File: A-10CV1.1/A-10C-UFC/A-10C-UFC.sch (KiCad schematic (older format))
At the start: 42 parts, among them J1 Conn_01x08_MountingPin, J2 Conn_01x10_MountingPin, J3 Conn_01x06_MountingPin, J4 Conn_01x15_Female, J5 Conn_01x15_Female, SW1 SW_Push, SW10 SW_Push, SW11 SW_Push, SW12 SW_Push, SW13 SW_Push, SW14 SW_Push, SW15 SW_Push, SW16 SW_Push, SW17 SW_Push, SW18 SW_Push, SW19 SW_Push, SW2 SW_Push, SW20 SW_Push, SW21 SW_Push, SW22 SW_Push, SW23 SW_Push, SW24 SW_Push, SW25 SW_Push, SW26 SW_Push, SW27 SW_Push, SW28 SW_Push, SW29 SW_Push, SW3 SW_Push, SW30 SW_Push, SW31 SW_Push, SW32 SW_Push, SW33 SW_Push, SW34 SW_Push, SW35 SW_Push, SW4 SW_Push, SW5 SW_Push, SW6 SW_Push, SW7 SW_Push, SW8 SW_Push, SW9 SW_Push

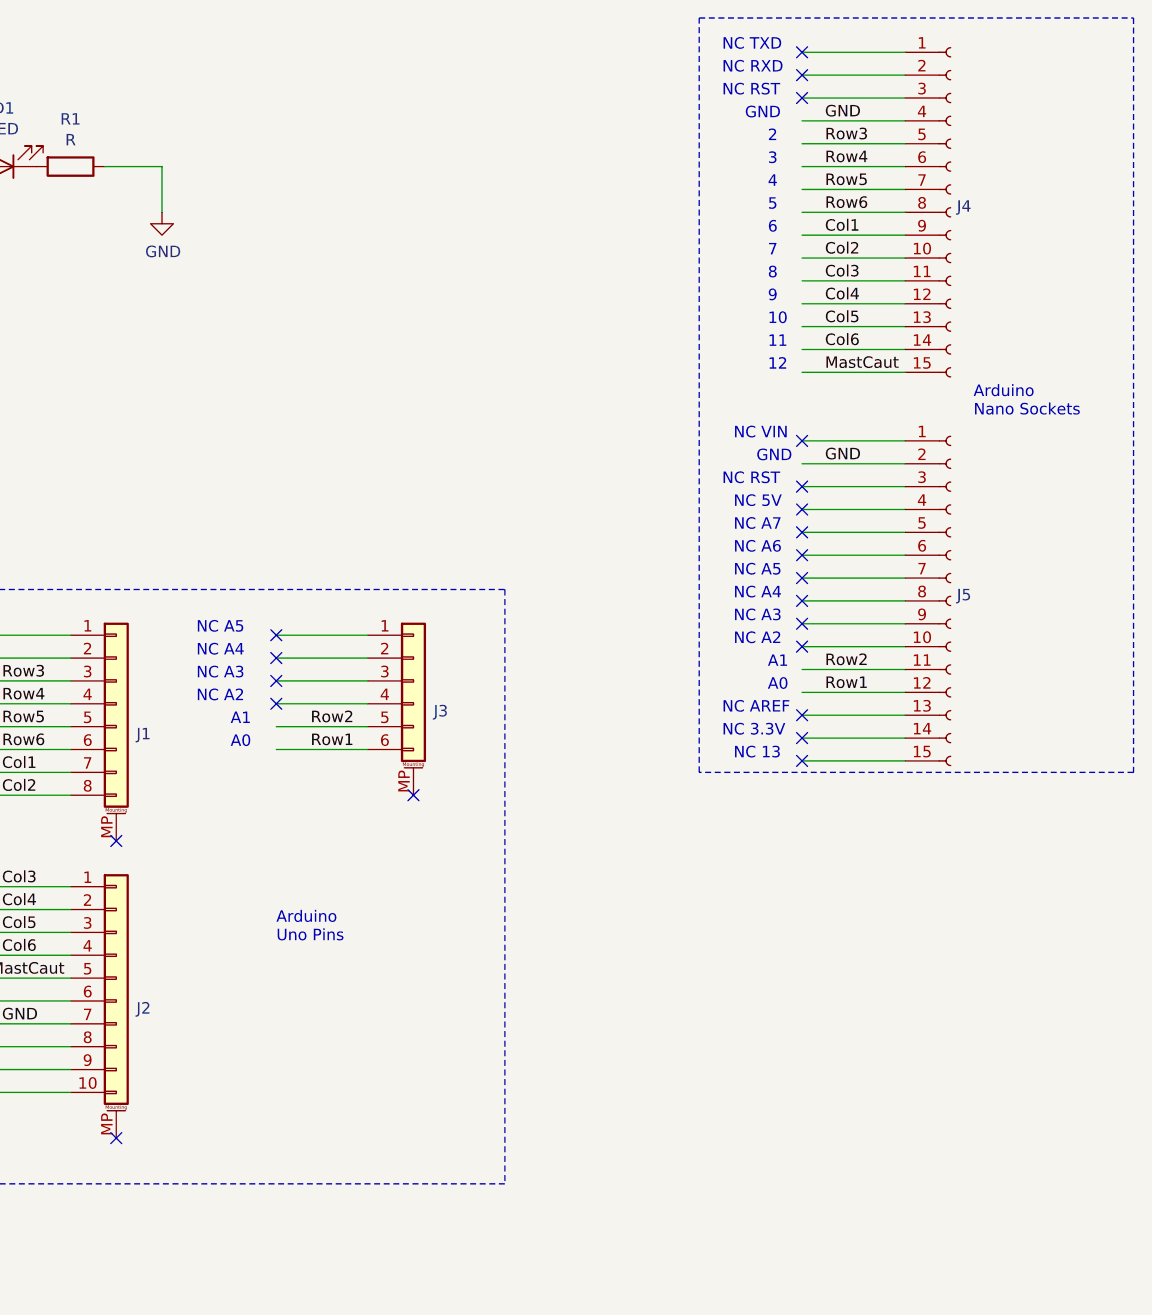
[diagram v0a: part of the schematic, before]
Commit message: Updated for multi aircraft capability.  Added wiring and code.
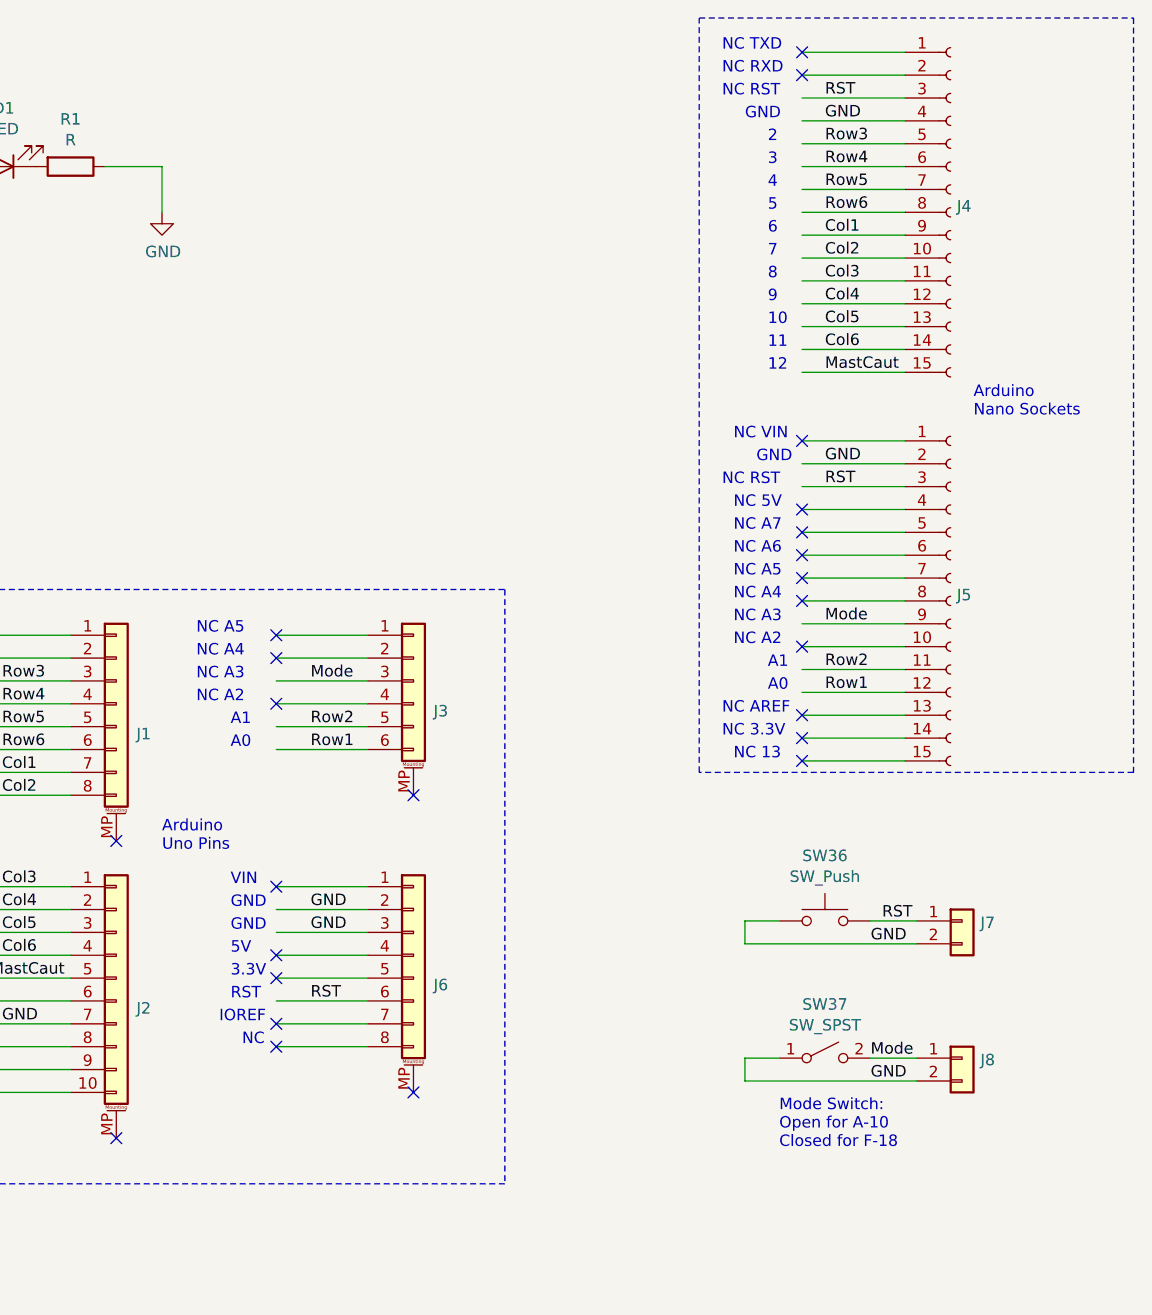
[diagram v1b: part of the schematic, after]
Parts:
- added J6: Conn_01x08_MountingPin, Connector_PinHeader_2.54mm:PinHeader_1x08_P2.54mm_Vertical, symbol Connector_Generic_MountingPin:Conn_01x08_MountingPin
- added J7, J8: Conn_01x02, Connector_JST:JST_XH_B02B-XH-A_1x02_P2.50mm_Vertical, symbol Connector_Generic:Conn_01x02
- added SW36: SW_Push, symbol Switch:SW_Push
- added SW37: SW_SPST, symbol Switch:SW_SPST
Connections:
- net labels added: Mode, RST
- wire segments 162 -> 178
- no-connect marks 28 -> 30
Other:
- note added: "3.3V"
- note added: "5V"
- note added: "IOREF"
- note added: "Mode Switch:\nOpen for A-10\nClosed for F-18"
- note added: "NC"
- note added: "RST"
- note added: "VIN"
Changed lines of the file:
@@
 Wire Notes Line
 	6500 5900 6500 3300
-Text Notes 8300 4850 0    50   ~ 0
+Text Notes 7800 4450 0    50   ~ 0
 Arduino\nUno Pins
 Text Notes 3200 6750 0    50   ~ 0
 Row  Digital Pins (A0,A1,2,3,4,5)\nCol Digital Pins (6,7,8,9,10,11)\n\nLED Output for Master Caution, Pin 12\n\nDesigned for plug in compatibility with \nArduino UNO and Nano
 NoConn ~ 10600 2650
-NoConn ~ 10600 2850
 NoConn ~ 10600 2950
 NoConn ~ 10600 3050
@@
 NoConn ~ 10600 3250
 NoConn ~ 10600 3350
-NoConn ~ 10600 3450
 NoConn ~ 10600 3550
 NoConn ~ 10600 3850
@@
 NoConn ~ 10600 950
 NoConn ~ 10600 1050
-NoConn ~ 10600 1150
 NoConn ~ 7000 3500
 NoConn ~ 7000 3600
 NoConn ~ 8300 3500
 NoConn ~ 8300 3600
-NoConn ~ 8300 3700
 NoConn ~ 8300 3800
 NoConn ~ 7600 4400
@@
 NoConn ~ 7000 5300
 NoConn ~ 7000 5100
+$Comp
+L Connector_Generic:Conn_01x02 J7
+U 1 1 5D473A0F
+P 11300 4750
+F 0 "J7" H 11380 4742 50  0000 L CNN
+F 1 "Conn_01x02" H 11380 4651 50  0001 L CNN
+F 2 "Connector_JST:JST_XH_B02B-XH-A_1x02_P2.50mm_Vertical" H 11300 4750 50  0001 C CNN
+F 3 "~" H 11300 4750 50  0001 C CNN
+	1    11300 4750
+	1    0    0    -1
+$EndComp
+$Comp
+L Connector_Generic:Conn_01x02 J8
+U 1 1 5D473B23
+P 11300 5350
+F 0 "J8" H 11380 5342 50  0000 L CNN
+F 1 "Conn_01x02" H 11380 5251 50  0001 L CNN
+F 2 "Connector_JST:JST_XH_B02B-XH-A_1x02_P2.50mm_Vertical" H 11300 5350 50  0001 C CNN
+F 3 "~" H 11300 5350 50  0001 C CNN
+	1    11300 5350
+	1    0    0    -1
+$EndComp
+$Comp
+L Switch:SW_Push SW36
+U 1 1 5D473BB8
+P 10700 4750
+F 0 "SW36" H 10700 5035 50  0000 C CNN
+F 1 "SW_Push" H 10700 4944 50  0000 C CNN
+F 2 "" H 10700 4950 50  0001 C CNN
+F 3 "" H 10700 4950 50  0001 C CNN
+	1    10700 4750
+	1    0    0    -1
+$EndComp
+$Comp
+L Switch:SW_SPST SW37
+U 1 1 5D473C67
+P 10700 5350
+F 0 "SW37" H 10700 5585 50  0000 C CNN
+F 1 "SW_SPST" H 10700 5494 50  0000 C CNN
+F 2 "" H 10700 5350 50  0001 C CNN
+F 3 "" H 10700 5350 50  0001 C CNN
+	1    10700 5350
+	1    0    0    -1
+$EndComp
+Wire Wire Line
+	11100 4750 10900 4750
+Wire Wire Line
+	10350 4750 10350 4850
+Wire Wire Line
+	10350 4850 11100 4850
+Wire Wire Line
+	10350 4750 10500 4750
+Wire Wire Line
+	11100 5350 10900 5350
+Wire Wire Line
+	10500 5350 10350 5350
+Wire Wire Line
+	10350 5350 10350 5450
+Wire Wire Line
+	10350 5450 11100 5450
+Text Label 10900 5450 0    50   ~ 0
+GND
+Text Label 10900 4850 0    50   ~ 0
+GND
+$Comp
+L Connector_Generic_MountingPin:Conn_01x08_MountingPin J6
+U 1 1 5D4991C7
+P 8900 4900
+F 0 "J6" H 8988 4770 50  0000 L CNN
+F 1 "Conn_01x08_MountingPin" H 8987 4725 50  0001 L CNN
+F 2 "Connector_PinHeader_2.54mm:PinHeader_1x08_P2.54mm_Vertical" H 8900 4900 50  0001 C CNN
+F 3 "~" H 8900 4900 50  0001 C CNN
+	1    8900 4900
+	1    0    0    -1
+$EndComp
+Wire Wire Line
+	8700 5100 8300 5100
+Wire Wire Line
+	8700 5000 8300 5000
+Wire Wire Line
+	8700 4900 8300 4900
+Wire Wire Line
+	8700 4800 8300 4800
+Wire Wire Line
+	8700 4700 8300 4700
+Wire Wire Line
+	8700 4600 8300 4600
+Wire Wire Line
+	8700 5200 8300 5200
+Wire Wire Line
+	8700 5300 8300 5300
+Text Label 8450 5100 0    50   ~ 0
+RST
+NoConn ~ 8300 5200
+NoConn ~ 8300 5300
+NoConn ~ 8300 5000
+NoConn ~ 8300 4900
+NoConn ~ 8300 4600
+NoConn ~ 8900 5500
+Text Label 10950 4750 0    50   ~ 0
+RST
+Text Notes 10500 5750 0    50   ~ 0
+Mode Switch:\nOpen for A-10\nClosed for F-18
+Text Label 8450 3700 0    50   ~ 0
+Mode
+Text Label 10900 5350 0    50   ~ 0
+Mode
+Text Label 10700 3450 0    50   ~ 0
+Mode
+Text Label 10700 2850 0    50   ~ 0
+RST
+Text Label 10700 1150 0    50   ~ 0
+RST
+Text Label 8450 4700 0    50   ~ 0
+GND
+Text Label 8450 4800 0    50   ~ 0
+GND
+Text Notes 8100 4600 0    50   ~ 0
+VIN
+Text Notes 8100 4700 0    50   ~ 0
+GND
+Text Notes 8100 4800 0    50   ~ 0
+GND
+Text Notes 8100 4900 0    50   ~ 0
+5V
+Text Notes 8100 5000 0    50   ~ 0
+3.3V
+Text Notes 8100 5100 0    50   ~ 0
+RST
+Text Notes 8050 5200 0    50   ~ 0
+IOREF
+Text Notes 8150 5300 0    50   ~ 0
+NC
 $EndSCHEMATC
